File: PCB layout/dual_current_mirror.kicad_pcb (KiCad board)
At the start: 2 copper layers, 150 x 100 mm, 36 parts, among them J1 9.8V INPUT, J101 9.8V INPUT, J102 RLOAD VOLTAGE, J103 Q101 BASE-EMITTER, J104 Q102 BASE-EMITTER, J2 RLOAD VOLTAGE, J3 Q1 BASE-EMITTER, J4 Q2 BASE-EMITTER, Q1 2N3904, Q101 2N3904, Q102 2N3904, Q2 2N3904

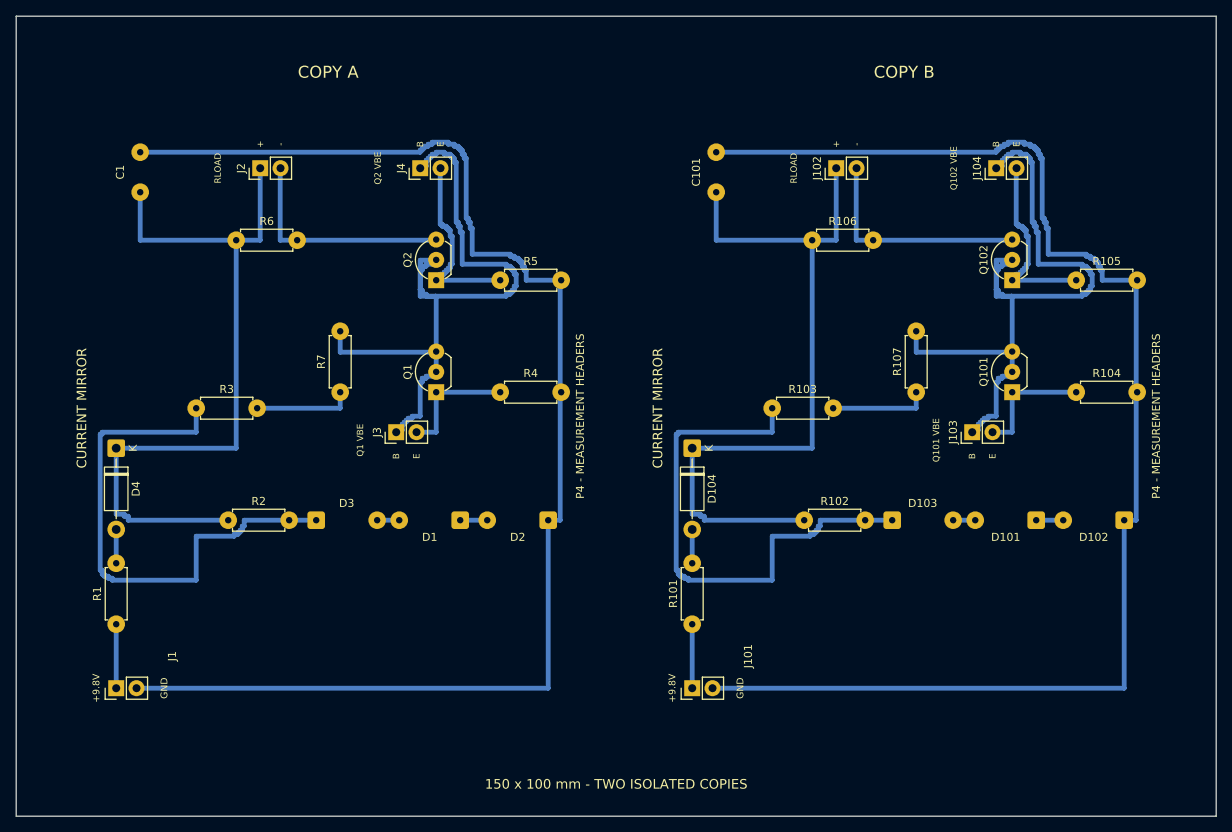
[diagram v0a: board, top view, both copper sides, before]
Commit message: Increase soldering clearance on both current mirror copies
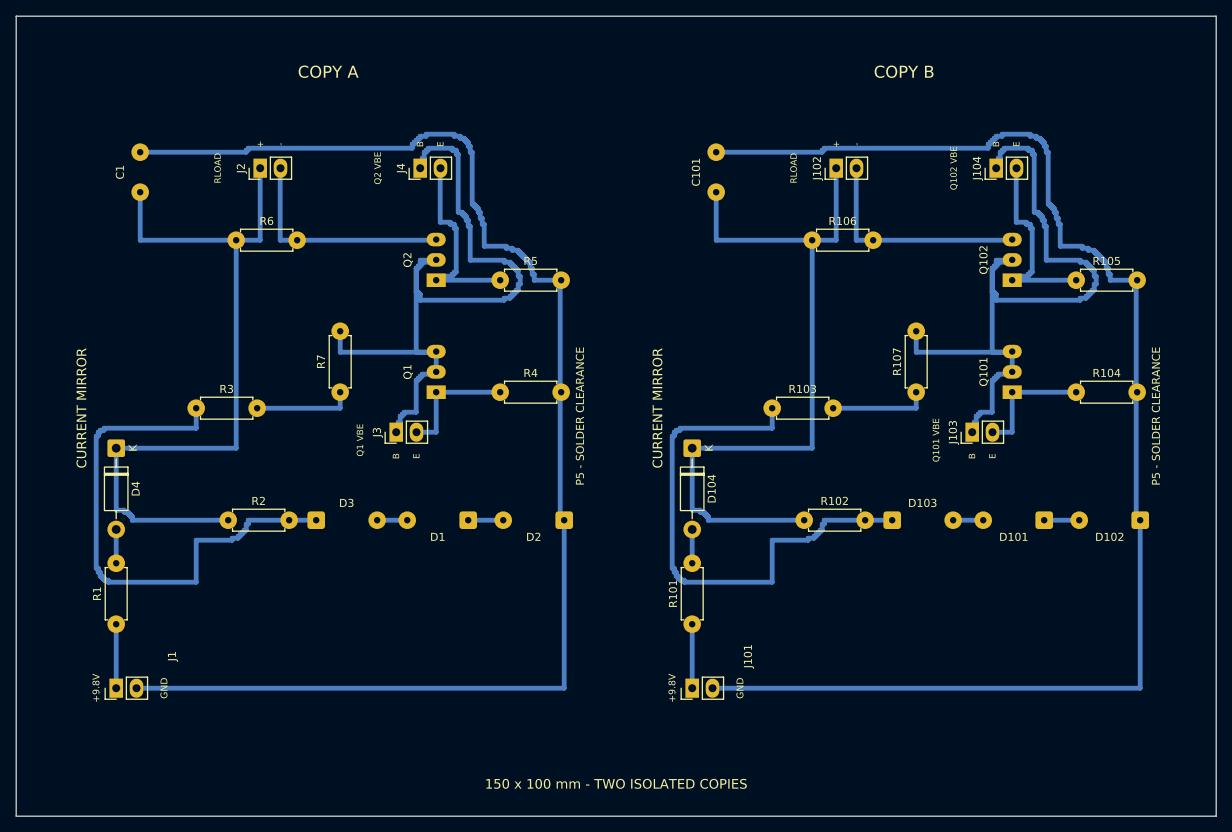
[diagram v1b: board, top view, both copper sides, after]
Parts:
- moved D102 2.00 mm to (140.5, 63.0)
- moved D2 2.00 mm to (68.5, 63.0)
- moved D1 1.00 mm to (56.5, 63.0)
- moved D101 1.00 mm to (128.5, 63.0)
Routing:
- net /B_BASE: track 96.0 -> 101.0 mm
- net /A_BASE: track 96.0 -> 101.0 mm
- net /B_GND: track 175.5 -> 178.5 mm
- net /A_GND: track 175.5 -> 178.5 mm
- net /B_VA: track 68.2 -> 69.7 mm
- net /A_VA: track 68.2 -> 69.7 mm
- net /B_ZD_A: track 3.24 -> 4.24 mm
- net /B_E2: track 25.5 -> 26.5 mm
- net /B_D12: track 3.62 -> 4.62 mm
- net /A_ZD_A: track 3.24 -> 4.24 mm
- net /A_E2: track 25.5 -> 26.5 mm
- net /A_D12: track 3.62 -> 4.62 mm
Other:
- board text added: "P5 - SOLDER CLEARANCE"
- board text removed: "P4 - MEASUREMENT HEADERS"

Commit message: Restore P6 PCB layout and retain centre-cut manufacturing setup
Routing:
- net /B_VA: track 69.7 -> 22.3 mm
- net /A_VA: track 69.7 -> 22.3 mm
- net /B_BASE: track 101.0 -> 56.9 mm
- net /A_BASE: track 101.0 -> 56.9 mm
- net /A_GND: track 178.5 -> 153.9 mm
- net /B_GND: track 178.5 -> 153.9 mm
- net /B_VCC: track 94.0 -> 74.7 mm
- net /A_VCC: track 94.0 -> 74.7 mm
- net /A_OUT: track 28.9 -> 27.3 mm
- net /B_OUT: track 28.9 -> 27.3 mm
- net /A_E1: track 15.5 -> 14.0 mm
- net /B_E1: track 15.5 -> 14.0 mm
- net /B_TRIM_TOP: track 12.6 -> 11.3 mm
- net /A_TRIM_TOP: track 12.6 -> 11.3 mm
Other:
- board text added: "CENTRE CUT: X=75 mm"
- board text added: "P6 - STRAIGHT ROUTES"
- board text removed: "P5 - SOLDER CLEARANCE"
